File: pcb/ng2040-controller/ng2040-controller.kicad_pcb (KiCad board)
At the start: 2 copper layers, 67.5 x 35 mm, 17 parts, among them J1 A, J2 B, J3 C, J4 D, J5 START, J6 SELECT, J7 JOY, J8 BATTERY, SW1 OPTS, SW2 POWER, U1 RP2040-Zero, U2 NRF24L01

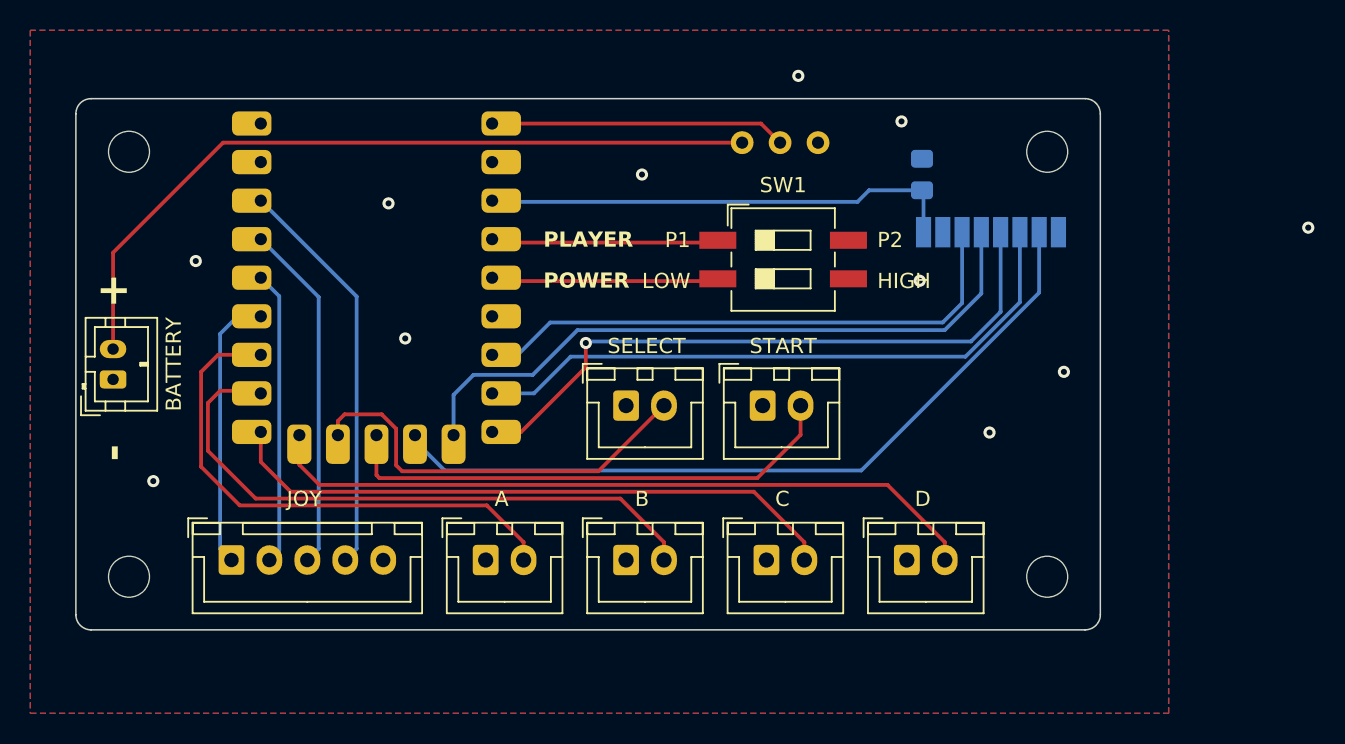
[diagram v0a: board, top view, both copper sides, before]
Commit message: WIP changing controller into a narrower one breaking away NRF
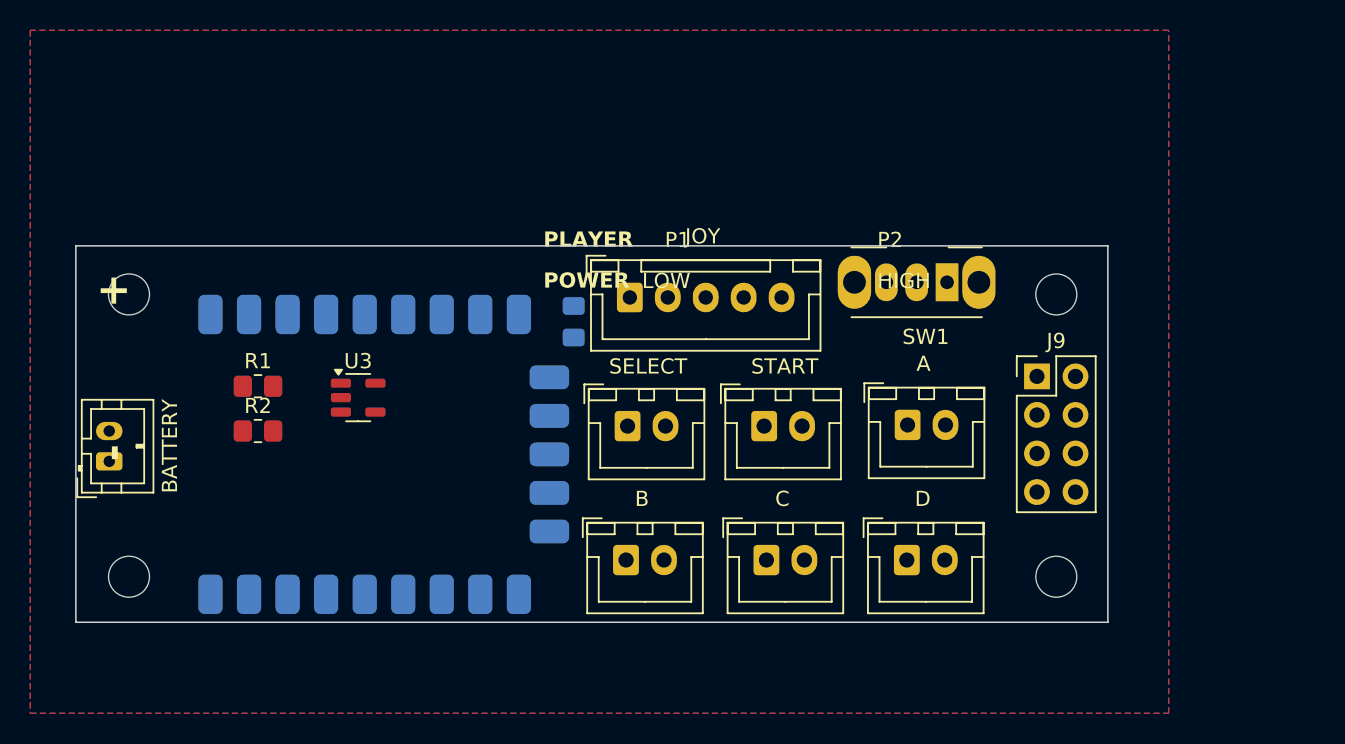
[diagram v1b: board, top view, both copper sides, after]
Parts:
- removed SW2: POWER, REB_Switch:REB_SlideSwitch_3pin
- removed U2: NRF24L01, NRF24L01:NRF24L01-SMD
- added J9: Conn_02x04_Counter_Clockwise, Connector_PinHeader_2.54mm:PinHeader_2x04_P2.54mm_Vertical, F.Cu at (101.3, 57.8)
- added R1: 100K, Resistor_SMD:R_0805_2012Metric_Pad1.20x1.40mm_HandSolder, F.Cu at (50.0, 58.5)
- added R2: 100K, Resistor_SMD:R_0805_2012Metric_Pad1.20x1.40mm_HandSolder, F.Cu at (50.0, 61.4)
- added U3: MIC5205-3.0YM5, Package_TO_SOT_SMD:SOT-23-5, F.Cu at (56.6, 59.2)
- SW1: footprint Button_Switch_SMD:SW_DIP_SPSTx02_Slide_6.7x6.64mm_W8.61mm_P2.54mm_LowProfile -> Button_Switch_THT:SW_Slide_SPDT_Angled_CK_OS102011MA1Q
- moved J7 31.4 mm to (74.5, 52.6)
- moved J1 29.2 mm to (92.8, 61.0)
- moved C1 24.9 mm to (70.8, 54.2)
- moved U1 11.4 mm to (69.7, 52.8), turned to -90 degrees
- moved SW1 10.9 mm to (95.4, 51.6), turned to 180 degrees
- moved H3 9.42 mm to (102.6, 52.4)
- moved H4 9.40 mm to (41.5, 52.4)
- moved J8 5.41 mm to (40.2, 63.4)
- moved J5 1.35 mm to (83.3, 61.1)
- moved J6 1.35 mm to (74.3, 61.1)
- moved H1 0.60 mm to (102.6, 71.0)
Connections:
- C1 pad 1: /3V3 -> /3V0
- U1 pad 1: unconnected-(U1-GP0-Pad1) -> /RADIO_EN
- U1 pad 18: unconnected-(U1-GP27-Pad18) -> /BAT_SENSE
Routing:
- net /MISO: track 51.1 -> 0.00 mm
- net Net-(J8-Pin_2): track 50.8 -> 0.00 mm
- net /BD: track 47.8 -> 0.00 mm
- net /CS: track 44.2 -> 0.00 mm
- net /SCK: track 43.0 -> 0.00 mm, vias 1 -> 0
- net /MOSI: track 41.9 -> 0.00 mm
- net /BC: track 41.2 -> 0.00 mm
- net /BB: track 40.8 -> 0.00 mm
- net /CE: track 37.0 -> 0.00 mm
- net /BA: track 35.1 -> 0.00 mm
- net /STA: track 33.8 -> 0.00 mm
- net /3V3: track 31.5 -> 0.00 mm
- net /SEL: track 27.4 -> 0.00 mm
- net /DL: track 26.6 -> 0.00 mm
- net /DR: track 23.0 -> 0.00 mm
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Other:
- board size 67.5 x 35 mm -> 68 x 24.8 mm

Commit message: Revise controller pcb, still use RP2040 but break out to radio daughterboard pointing up
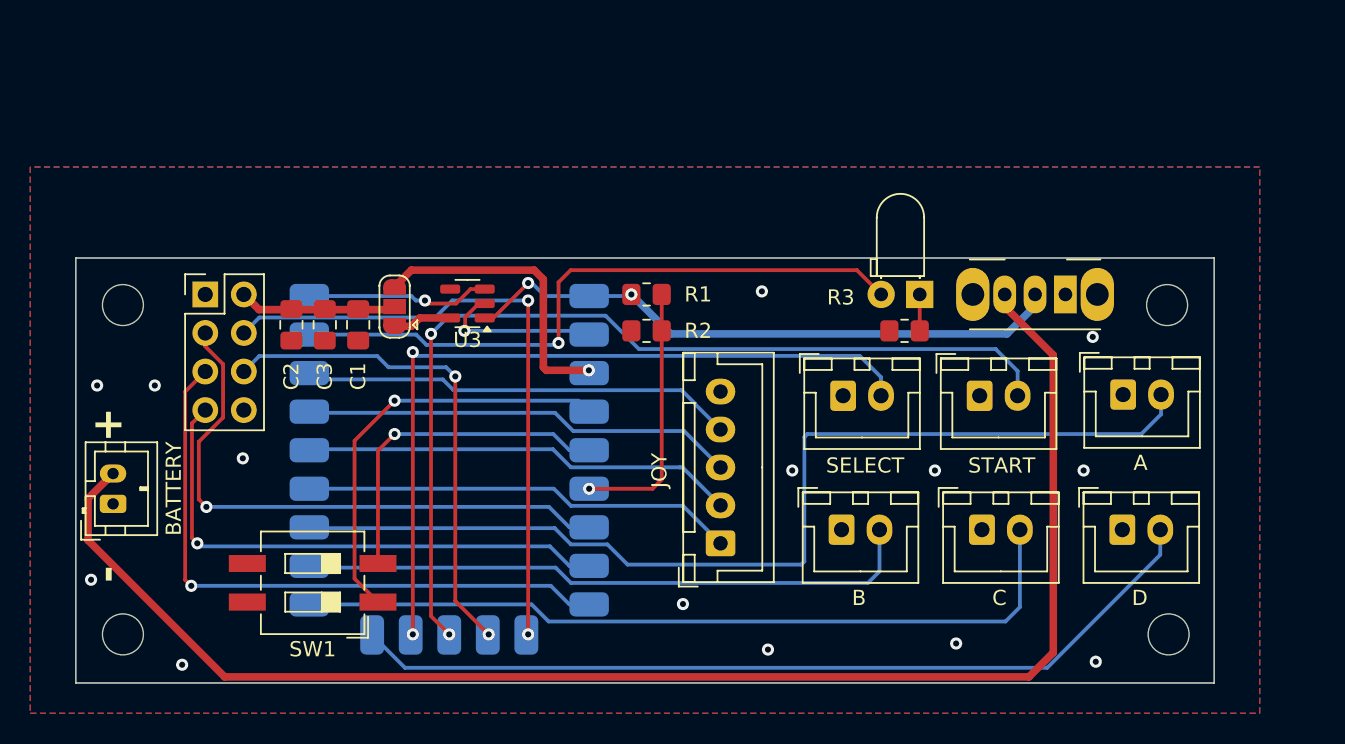
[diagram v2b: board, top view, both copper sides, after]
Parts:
- added C2: 0.1uF, Capacitor_SMD:C_0805_2012Metric_Pad1.18x1.45mm_HandSolder, F.Cu at (52.2, 54.4)
- added C3: 100nF, Capacitor_SMD:C_0805_2012Metric_Pad1.18x1.45mm_HandSolder, F.Cu at (54.4, 54.4)
- added D1: LED, LED_THT:LED_D3.0mm_Horizontal_O1.27mm_Z6.0mm, F.Cu at (93.6, 52.4)
- added JP1: Radio PWR select, Jumper:SolderJumper-3_P1.3mm_Open_RoundedPad1.0x1.5mm, F.Cu at (59.0, 53.2)
- added R3: 1K, Resistor_SMD:R_0805_2012Metric_Pad1.20x1.40mm_HandSolder, F.Cu at (92.6, 54.8)
- added SW2: POWER, Button_Switch_THT:SW_Slide_SPDT_Angled_CK_OS102011MA1Q, F.Cu at (103.2, 52.4)
- C1: value 1uF -> 10uF; moved to F.Cu
- J9: value Conn_02x04_Counter_Clockwise -> NRF24L01 Connector
- SW1: footprint Button_Switch_THT:SW_Slide_SPDT_Angled_CK_OS102011MA1Q -> Button_Switch_SMD:SW_DIP_SPSTx02_Slide_6.7x6.64mm_W8.61mm_P2.54mm_LowProfile
- moved J9 55.1 mm to (46.5, 52.4)
- moved SW1 46.3 mm to (53.6, 71.4)
- moved R2 26.4 mm to (75.6, 54.8), turned to 180 degrees
- moved R1 26.3 mm to (75.6, 52.4), turned to 180 degrees
- moved U1 22.8 mm to (72.8, 75.4), turned to 180 degrees
- moved J7 17.3 mm to (80.5, 68.8), turned to 90 degrees
- moved J1 14.3 mm to (107.0, 59.0)
- moved J2 14.3 mm to (88.5, 67.9)
- moved J3 14.3 mm to (97.7, 67.9)
- moved J4 14.3 mm to (107.0, 67.9)
- moved J5 14.3 mm to (97.5, 59.1)
- moved J6 14.3 mm to (88.5, 59.1)
- moved C1 14.2 mm to (56.6, 54.4)
- moved U3 9.50 mm to (63.8, 53.0), turned to 180 degrees
- moved H1 8.32 mm to (110.0, 74.8)
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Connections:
- C1 pad 1: /3V0 -> GND
- C1 pad 2: GND -> Net-(J9-Pin_2)
- J9 pad 1: unconnected-(J9-Pin_1-Pad1) -> GND
- J9 pad 2: unconnected-(J9-Pin_2-Pad2) -> Net-(J9-Pin_2)
- J9 pad 3: unconnected-(J9-Pin_3-Pad3) -> /CE
- J9 pad 4: unconnected-(J9-Pin_4-Pad4) -> /CS
- J9 pad 5: unconnected-(J9-Pin_5-Pad5) -> /SCK
- J9 pad 6: unconnected-(J9-Pin_6-Pad6) -> /MISO
- J9 pad 7: unconnected-(J9-Pin_7-Pad7) -> /MOSI
- J9 pad 8: unconnected-(J9-Pin_8-Pad8) -> /IRQ
- U1 pad 2: unconnected-(U1-GP1-Pad2) -> /ACT_LED
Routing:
- net Net-(J8-Pin_2): track 0.00 -> 98.0 mm
- net /BA: track 0.00 -> 67.3 mm
- net /STA: track 0.00 -> 62.6 mm, vias 0 -> 2
- net /BD: track 0.00 -> 57.6 mm
- net /BC: track 0.00 -> 52.8 mm
- net /SEL: track 0.00 -> 51.4 mm, vias 0 -> 2
- net /ACT_LED: track 0.00 -> 43.0 mm, vias 0 -> 1
- net /CS: track 0.00 -> 41.6 mm, vias 0 -> 2
- net /SCK: track 0.00 -> 41.6 mm, vias 0 -> 1
- net /BB: track 0.00 -> 41.1 mm
- net /VBATT: track 0.00 -> 40.2 mm, vias 0 -> 2
- net /CE: track 0.00 -> 38.6 mm, vias 0 -> 1
- net /MOSI: track 0.00 -> 35.7 mm, vias 0 -> 1
- net /MISO: track 0.00 -> 32.8 mm, vias 0 -> 2
- net /DD: track 0.00 -> 28.7 mm
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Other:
- board size 68 x 24.8 mm -> 75 x 28 mm
- board text removed: "HIGH"
- board text removed: "LOW"
- board text removed: "OFF"
- board text removed: "ON"
- board text removed: "P1"
- board text removed: "P2"
- board text removed: "PLAYER"
- board text removed: "POWER"

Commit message: Fix issues with REV2
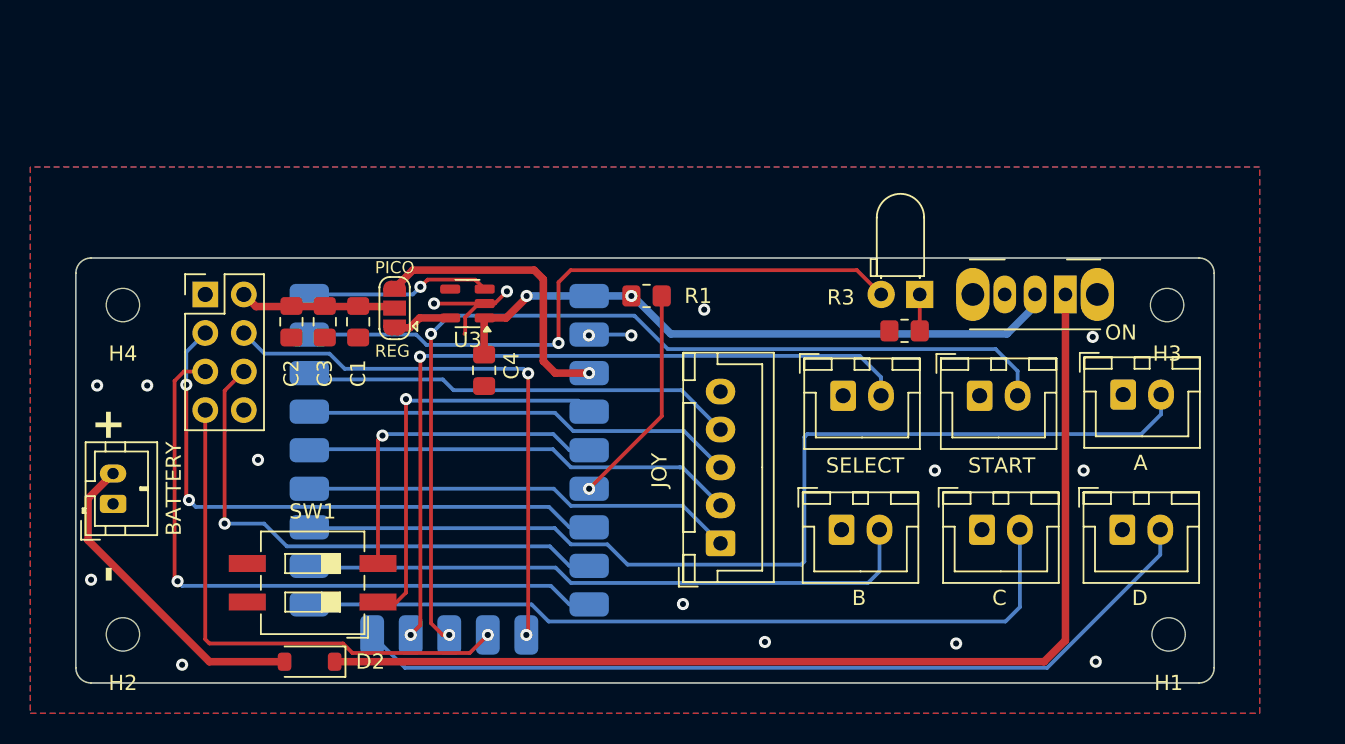
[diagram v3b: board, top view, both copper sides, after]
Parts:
- removed R2: 100K, Resistor_SMD:R_0805_2012Metric_Pad1.20x1.40mm_HandSolder
- added C4: 1uF, Capacitor_SMD:C_0805_2012Metric_Pad1.18x1.45mm_HandSolder, F.Cu at (64.9, 57.4)
- added D2: D_Schottky, Diode_SMD:D_SOD-123, F.Cu at (53.4, 76.6)
- H1, H2, H3, H4: value MountingHole_2.7mm_M2.5 -> MountingHole_2.2mm_M2; footprint MountingHole:MountingHole_2.7mm_M2.5 -> MountingHole:MountingHole_2.2mm_M2
- R1: value 100K -> 10K
- moved C1 0.20 mm to (56.6, 54.2)
- moved C2 0.20 mm to (52.2, 54.2)
- moved C3 0.20 mm to (54.4, 54.2)
- moved R1 0.10 mm to (75.6, 52.5)
- moved JP1 0.10 mm to (59.0, 53.3)
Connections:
- net /VBATT renamed /VIN
- J8 pad 2: Net-(J8-Pin_2) -> Net-(D2-A)
- J9 pad 6: /MISO -> /MOSI
- J9 pad 7: /MOSI -> /MISO
- SW2 pad 1: unconnected-(SW2-A-Pad1) -> Net-(D2-K)
- SW2 pad 3: Net-(J8-Pin_2) -> unconnected-(SW2-C-Pad3)
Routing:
- net Net-(J8-Pin_2): track 98.0 -> 0.00 mm
- net Net-(D2-K): track 0.00 -> 71.5 mm
- net Net-(D2-A): track 0.00 -> 21.3 mm
- net /CS: track 41.6 -> 37.1 mm
- net /BAT_SENSE: track 17.2 -> 14.7 mm
- net /MISO: track 32.8 -> 34.6 mm, vias 2 -> 1
- net /SCK: track 41.6 -> 43.3 mm
- net /VIN: track 40.2 -> 41.9 mm
- net /SET_PLAYER: track 28.1 -> 27.3 mm
- net unconnected-(SW2-C-Pad3): track 0.00 -> 0.80 mm
- net /SEL: track 51.4 -> 50.8 mm
- net GND: track 10.9 -> 11.3 mm, vias 15 -> 17
- net /CE: track 38.6 -> 38.7 mm, vias 1 -> 2
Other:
- outline, holes or cut-outs redrawn
- board text added: "ON"
- board text added: "PICO"
- board text added: "REG"

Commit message: Rev3 tweaks, ext LED
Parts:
- moved R3 12.2 mm to (80.6, 52.4)
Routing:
- net Net-(D1-K): track 2.40 -> 13.3 mm
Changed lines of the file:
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@@
 			(at 0 -3.2 180)
 			(layer "F.SilkS")
+			(hide yes)
 			(effects
 				(font
@@
 			(at 0 -3.2 180)
 			(layer "F.SilkS")
+			(hide yes)
 			(effects
 				(font
@@
 			(at 0 -3.2 180)
 			(layer "F.SilkS")
+			(hide yes)
 			(effects
 				(font
@@
 		(tags "resistor handsolder")
 		(property "Reference" "R1"
-			(at -3.4 0 0)
+			(at 0 -1.9 0)
 			(layer "F.SilkS")
 			(effects
@@
 			(at 0 -3.2 180)
 			(layer "F.SilkS")
+			(hide yes)
 			(effects
 				(font
@@
 	(footprint "Resistor_SMD:R_0805_2012Metric_Pad1.20x1.40mm_HandSolder"
 		(layer "F.Cu")
-		(at 92.6 54.8 180)
+		(at 80.6 52.4 180)
 		(descr "Resistor SMD 0805 (2012 Metric), square (rectangular) end terminal, IPC_7351 nominal with elongated pad for handsoldering. (Body size source: IPC-SM-782 page 72, https://www.pcb-3d.com/wordpress/wp-content/uploads/ipc-sm-782a_amendment_1_and_2.pdf), generated with kicad-footprint-generator")
 		(tags "resistor handsolder")
 		(property "Reference" "R3"
-			(at 4.2 2.2 0)
+			(at 0 -2 0)
 			(layer "F.SilkS")
 			(effects
@@
 		(model "${KICAD8_3DMODEL_DIR}/LED_THT.3dshapes/LED_D3.0mm_Horizontal_O1.27mm_Z6.0mm.wrl"
 			(offset
-				(xyz 0 0 -2)
+				(xyz 0 0 -3.5)
 			)
 			(scale
@@
 	)
 	(via
-		(at 79.4 53.4)
+		(at 86.6 52.4)
 		(size 0.8)
 		(drill 0.4)
@@
 	)
 	(segment
-		(start 63.950001 76.025)
-		(end 65.14 74.835001)
+		(start 46.525 60.02)
+		(end 46.525 74.525)
 		(width 0.25)
 		(layer "F.Cu")
@@
 	)
 	(segment
-		(start 46.525 75.125)
-		(end 46.8 75.4)
+		(start 55.6 75.4)
+		(end 56.225 76.025)
 		(width 0.25)
 		(layer "F.Cu")
@@
 	)
 	(segment
-		(start 55.6 75.4)
-		(end 56.225 76.025)
+		(start 56.225 76.025)
+		(end 63.950001 76.025)
 		(width 0.25)
 		(layer "F.Cu")
@@
 	)
 	(segment
-		(start 56.225 76.025)
-		(end 63.950001 76.025)
+		(start 47.4 75.4)
+		(end 55.6 75.4)
 		(width 0.25)
 		(layer "F.Cu")
@@
 	)
 	(segment
-		(start 46.525 60.02)
-		(end 46.525 75.125)
+		(start 63.950001 76.025)
+		(end 65.14 74.835001)
 		(width 0.25)
 		(layer "F.Cu")
@@
 	)
 	(segment
-		(start 46.8 75.4)
-		(end 55.6 75.4)
+		(start 46.525 74.525)
+		(end 47.4 75.4)
 		(width 0.25)
 		(layer "F.Cu")
@@
 	)
 	(segment
-		(start 93.6 52.4)
-		(end 93.6 54.8)
+		(start 92 54)
+		(end 93.6 52.4)
+		(width 0.25)
+		(layer "F.Cu")
+		(net 26)
+	)
+	(segment
+		(start 81.6 52.4)
+		(end 83.2 54)
+		(width 0.25)
+		(layer "F.Cu")
+		(net 26)
+	)
+	(segment
+		(start 83.2 54)
+		(end 92 54)
 		(width 0.25)
 		(layer "F.Cu")

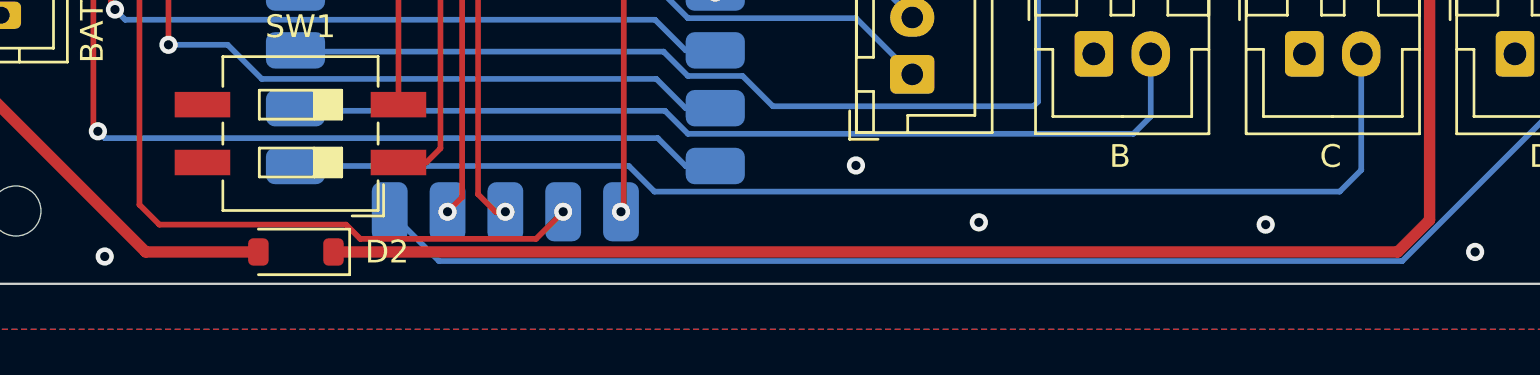
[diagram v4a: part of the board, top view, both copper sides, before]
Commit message: Remove diode as we don't want any more voltage drop
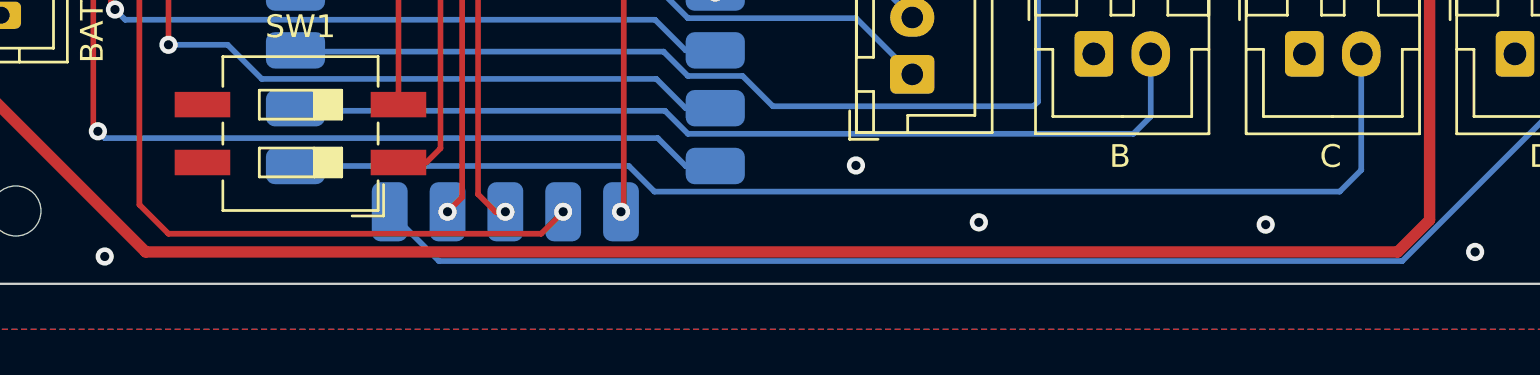
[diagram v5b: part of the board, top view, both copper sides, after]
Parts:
- removed D2: D_Schottky, Diode_SMD:D_SOD-123
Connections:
- J8 pad 2: Net-(D2-A) -> Net-(J8-Pin_2)
- SW2 pad 1: Net-(D2-K) -> Net-(J8-Pin_2)
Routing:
- net Net-(J8-Pin_2): track 0.00 -> 96.2 mm
- net Net-(D2-K): track 71.5 -> 0.00 mm
- net Net-(D2-A): track 21.3 -> 0.00 mm
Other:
- board text removed: "JLCJLCJLCJLC"
